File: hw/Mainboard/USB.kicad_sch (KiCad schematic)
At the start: 6 parts, among them J24 USB2.0_HOST_TYPE_C

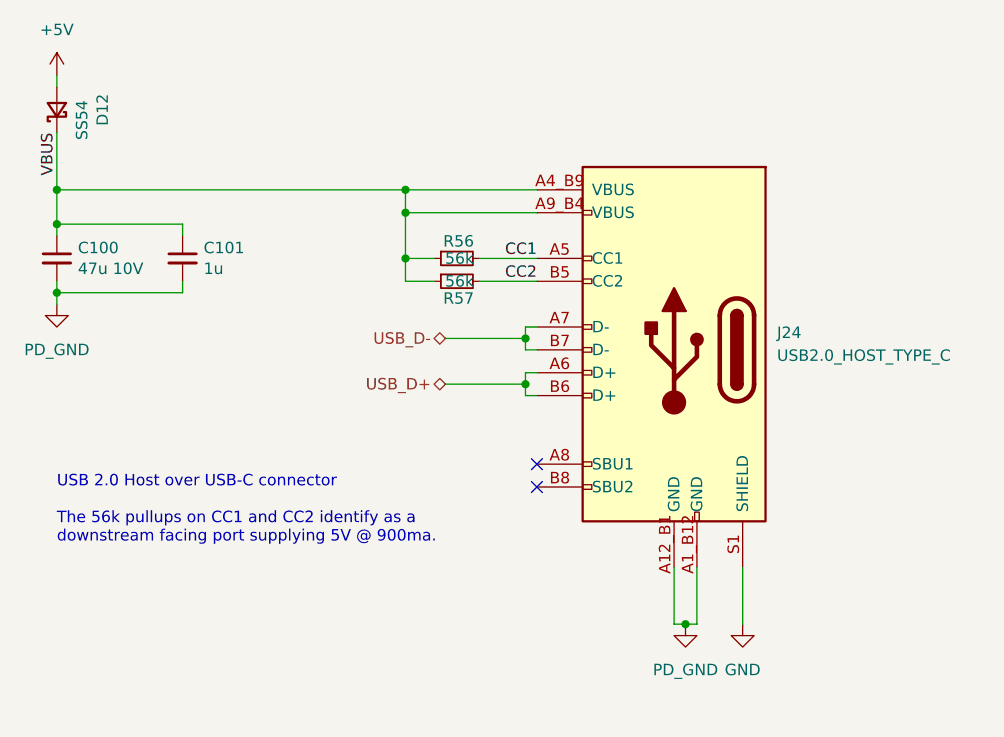
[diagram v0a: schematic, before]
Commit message: docs(hw): RP2040 PHY is USB 1.1 (not 2.0)
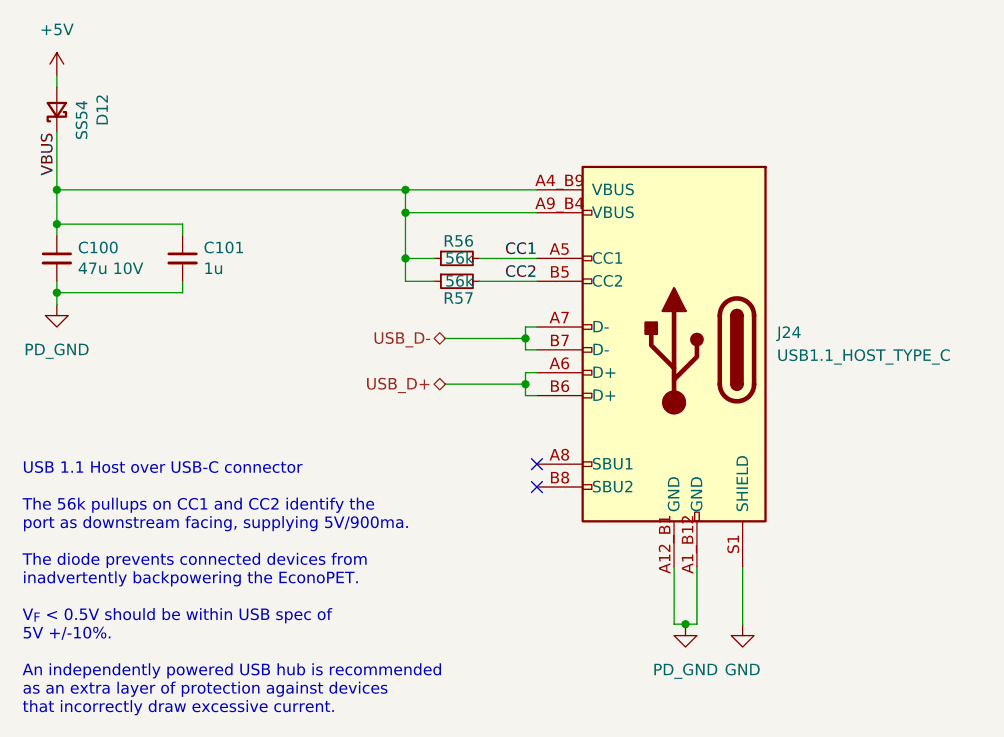
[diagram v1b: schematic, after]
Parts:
- J24: value USB2.0_HOST_TYPE_C -> USB1.1_HOST_TYPE_C
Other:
- note added: "USB 1.1 Host over USB-C connector The 56k pullups on CC1 and CC2 identify the port as downstream facing, supplying 5V/900ma. The diode prevents connected devices from inadvertently backpowering the EconoPET. V_{F} < 0.5V should be within USB spec of 5V +/-10%. An independently powered USB hub is recommended as an extra layer of protection against devices that incorrectly draw excessive current."
- note removed: "USB 2.0 Host over USB-C connector The 56k pullups on CC1 and CC2 identify as a downstream facing port supplying 5V @ 900ma."
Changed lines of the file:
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@@
     (stroke (width 0) (type default) (color 0 0 0 0))
   )
-  (text "USB 2.0 Host over USB-C connector\n\nThe 56k pullups on CC1 and CC2 identify as a\ndownstream facing port supplying 5V @ 900ma."
-    (at 83.82 114.3 0)
+  (text "USB 1.1 Host over USB-C connector\n\nThe 56k pullups on CC1 and CC2 identify the\nport as downstream facing, supplying 5V/900ma.\n\nThe diode prevents connected devices from\ninadvertently backpowering the EconoPET.\n\nV_{F} < 0.5V should be within USB spec of\n5V +/-10%.\n\nAn independently powered USB hub is recommended\nas an extra layer of protection against devices\nthat incorrectly draw excessive current.\n"
+    (at 80.01 133.35 0)
     (effects (font (size 1.27 1.27)) (justify left bottom))
   )
@@
       (effects (font (size 1.27 1.27)) (justify right))
     )
-    (property "Value" "USB2.0_HOST_TYPE_C" (id 1) (at 163.83 93.3449 0)
+    (property "Value" "USB1.1_HOST_TYPE_C" (id 1) (at 163.83 93.3449 0)
       (effects (font (size 1.27 1.27)) (justify right))
     )
